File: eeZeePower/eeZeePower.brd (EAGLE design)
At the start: 25.9 x 12.7 mm, 11 parts

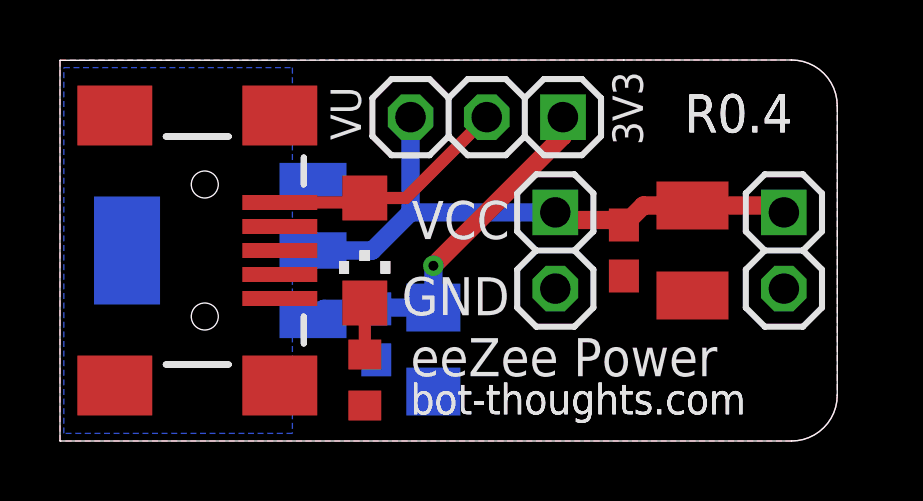
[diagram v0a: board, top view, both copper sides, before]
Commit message: Changed to 10mil/8mil spacing, improved thermal design, connected heatsink to VOUT.
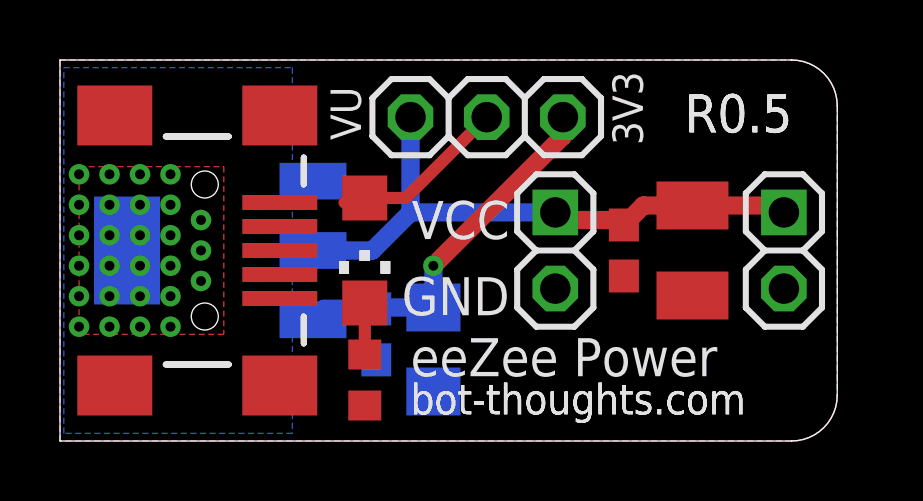
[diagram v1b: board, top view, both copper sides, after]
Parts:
- C1: value 0.1uF -> 10uF; device rcl:C0603 -> rcl:C1206
- C2: value 100uF -> 0.1uF; device rcl:SMC_B -> rcl:C0603
- C3: value 10uF -> 0.1uF; device rcl:C1206 -> rcl:C0603
- C4: value 0.1uF -> 100uF; device rcl:C0603 -> rcl:SMC_B
- U$1: value USBSMD -> USB-MINIB-5PIN
- moved C2 10.9 mm to (10.5, 3.56), flipped to the bottom
- moved C3 7.16 mm to (18.8, 6.35), flipped to the top
- moved C4 2.29 mm to (21.1, 6.35)
- moved C1 1.97 mm to (12.4, 3.05)
- renumbered JP1 to U$1
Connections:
- removed net HEATSINK: U1.4
- net GND: now also C2.2, C4.-, U$1.MTN1, U$1.MTN2, U$1.MTN3, U$1.MTN4; no longer C2.-, C4.2
- net VIN: now also C2.1; no longer C3.1
- net VOUT: now also C3.1, C4.+, U1.4; no longer C2.+, C4.1
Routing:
- net VBUS: track 8.03 -> 5.87 mm
- net VOUT: vias 0 -> 27
- added copper zone on layer 1, net VOUT
- added copper zone on layer 16, net VOUT
- removed copper zone on layer 16, net HEATSINK
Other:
- outline, holes or cut-outs redrawn
- board text added: "R0.5"
- board text removed: "R0.4"
